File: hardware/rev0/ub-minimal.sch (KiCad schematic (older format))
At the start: 1 part, among them P1 ANT

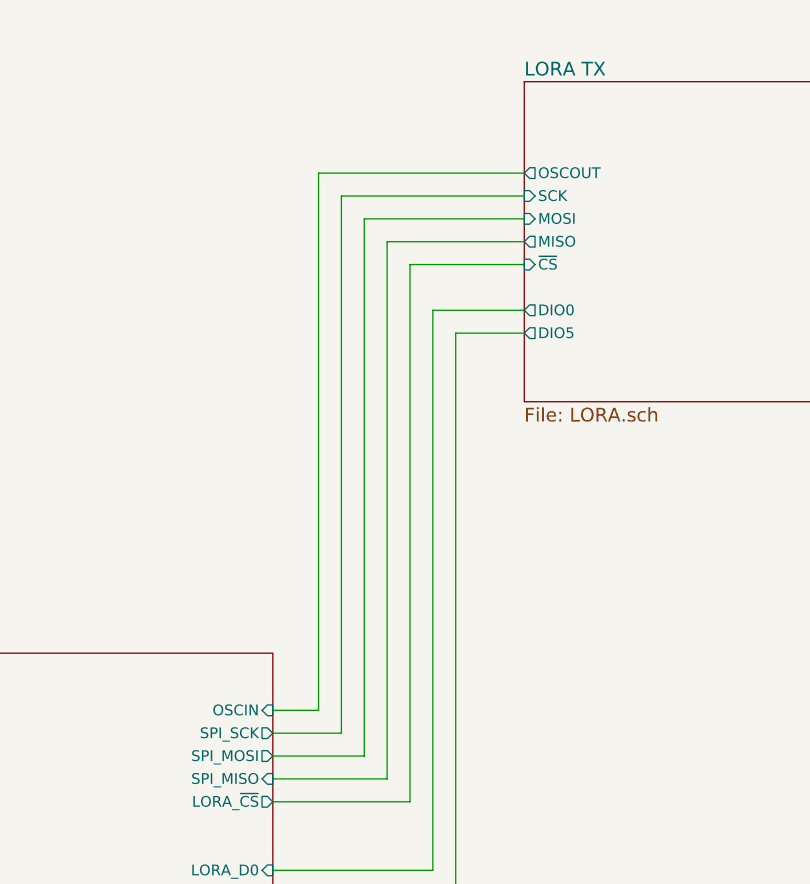
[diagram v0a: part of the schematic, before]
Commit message: DRC alterations, generate gerbers
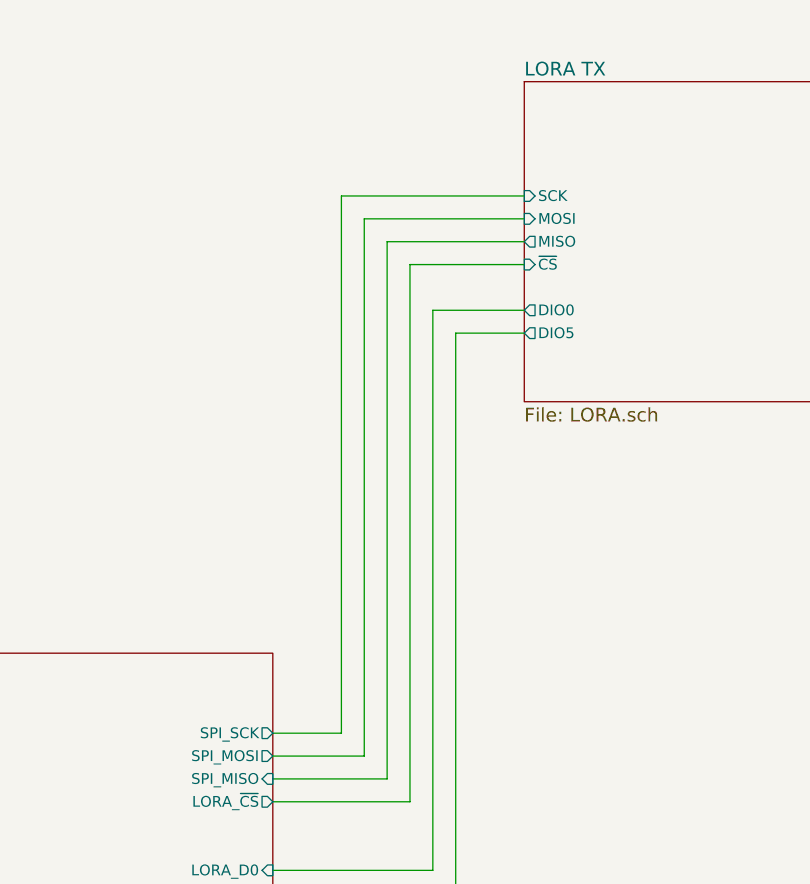
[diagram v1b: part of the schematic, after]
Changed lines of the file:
@@
 F7 "DIO5" O L 5800 2600 47
 F8 "ANT" O R 7350 1800 47
-F9 "OSCOUT" O L 5800 1900 47
 $EndSheet
 $Comp
@@
 F10 "I2C_SDA" B L 3000 4900 47
 F11 "I2C_SCL" O L 3000 4800 47
-F12 "OSCIN" I R 4700 4250 47
 $EndSheet
-Wire Wire Line
-	5800 1900 4900 1900
-Wire Wire Line
-	4900 1900 4900 4250
-Wire Wire Line
-	4900 4250 4700 4250
 $EndSCHEMATC
